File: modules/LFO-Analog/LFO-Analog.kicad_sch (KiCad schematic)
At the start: 56 parts, among them Q1 2N3904, Q2 2N3904, Q3 2N3904, Q4 2N3904, U1 TL074, U2 TL074

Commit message: LFO-Analog: BOM testing - it works!
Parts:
- RV1, RV2: Label (none) -> [label]
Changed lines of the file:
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@@
 			)
 		)
-		(property "Description" ""
+		(property "Description" "Resistor"
 			(at 207.01 38.1 0)
 			(effects
@@
 			)
 		)
-		(property "Description" ""
+		(property "Description" "Resistor"
 			(at 143.51 124.46 0)
 			(effects
@@
 			)
 		)
-		(property "Description" ""
+		(property "Description" "Resistor"
 			(at 143.51 40.64 0)
 			(effects
@@
 			)
 		)
-		(property "Description" ""
+		(property "Description" "Resistor"
 			(at 153.67 40.64 0)
 			(effects
@@
 			)
 		)
-		(property "Description" ""
+		(property "Description" "Small Signal NPN Transistor, 0.2A Ic, 40V Vce, TO-92"
 			(at 140.97 139.7 0)
 			(effects
@@
 			)
 		)
-		(property "Description" ""
+		(property "Description" "Small Signal NPN Transistor, 0.2A Ic, 40V Vce, TO-92"
 			(at 156.21 139.7 0)
 			(effects
@@
 			)
 		)
-		(property "Description" ""
+		(property "Description" "Trim-potentiometer"
 			(at 148.59 76.2 0)
 			(effects
@@
 			)
 		)
-		(property "Label" ""
+		(property "Label" "[label]"
 			(at 148.59 73.4639 90)
 			(effects
@@
 			)
 		)
-		(property "Description" ""
+		(property "Description" "Resistor"
 			(at 207.01 116.84 0)
 			(effects
@@
 			)
 		)
-		(property "Description" ""
+		(property "Description" "Resistor"
 			(at 207.01 33.02 0)
 			(effects
@@
 			)
 		)
-		(property "Description" ""
+		(property "Description" "Resistor"
 			(at 148.59 85.09 0)
 			(effects
@@
 			)
 		)
-		(property "Description" ""
+		(property "Description" "Resistor"
 			(at 161.29 146.05 0)
 			(effects
@@
 			)
 		)
-		(property "Description" ""
+		(property "Description" "Small Signal NPN Transistor, 0.2A Ic, 40V Vce, TO-92"
 			(at 156.21 55.88 0)
 			(effects
@@
 			)
 		)
-		(property "Description" ""
+		(property "Description" "Trim-potentiometer"
 			(at 148.59 160.02 0)
 			(effects
@@
 			)
 		)
-		(property "Label" ""
+		(property "Label" "[label]"
 			(at 148.59 157.2839 90)
 			(effects
@@
 			)
 		)
-		(property "Description" ""
+		(property "Description" "Resistor"
 			(at 161.29 62.23 0)
 			(effects
@@
 			)
 		)
-		(property "Description" ""
+		(property "Description" "Resistor"
 			(at 207.01 121.92 0)
 			(effects
@@
 			)
 		)
-		(property "Description" ""
+		(property "Description" "Resistor"
 			(at 153.67 124.46 0)
 			(effects
@@
 			)
 		)
-		(property "Description" ""
+		(property "Description" "Small Signal NPN Transistor, 0.2A Ic, 40V Vce, TO-92"
 			(at 140.97 55.88 0)
 			(effects
@@
 			)
 		)
-		(property "Description" ""
+		(property "Description" "Resistor"
 			(at 148.59 168.91 0)
 			(effects

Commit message: LFO-Analog: BOM testing - update some fields
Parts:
- RV1, RV2: Label [label] -> SINE-ADJ
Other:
- moved on the sheet: R11, R31, RV1, RV2

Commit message: LFO-Analog: BOM - done
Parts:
- C1, C5: Distributor (none) -> Mouser; DistributorPartLink (none) -> https://www.mouser.ca/ProductDetail/KEMET/R82EC1330JE50J?qs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; DistributorPartNum (none) -> 80-R82EC1330JE50J; Manufacturer (none) -> KEMET; ManufacturerPartNum (none) -> R82EC1330JE50J; Note PPS for best results -> (none)
- C2, C6: Distributor (none) -> Mouser; DistributorPartLink (none) -> https://www.mouser.ca/ProductDetail/KEMET/R82DC3680Z360K?qs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; DistributorPartNum (none) -> 80-R82DC3680Z360K; Manufacturer (none) -> KEMET; ManufacturerPartNum (none) -> R82DC3680Z360K; Note PPS for best results -> (none)
- C3, C7: Distributor (none) -> Mouser; DistributorPartLink (none) -> https://www.mouser.ca/ProductDetail/Vishay-BC-Components/K4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; DistributorPartNum (none) -> 594-K470J15C0GF53L2; Manufacturer (none) -> Vishay; ManufacturerPartNum (none) -> K470J15C0GF53L2
- C4, C8: Distributor (none) -> Mouser; DistributorPartLink (none) -> https://www.mouser.ca/ProductDetail/KEMET/R82EC1330JE50J?qs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; DistributorPartNum (none) -> 80-R82EC1330JE50J; Manufacturer (none) -> KEMET; ManufacturerPartNum (none) -> R82EC1330JE50J
- R1, R21: DistributorPartLink https://www.mouser.ca/c/?m=YAGEO&power+rating=166+mW+(1%2f6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 -> https://www.mouser.ca/ProductDetail/YAGEO/MFR-12FTF52-300K?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; DistributorPartNum 603-MFR-12* -> 603-MFR-12FTF52-300K; ManufacturerPartNum MFR-12* -> MFR-12FTF52-300K
- R10, R30: DistributorPartLink https://www.mouser.ca/c/?m=YAGEO&power+rating=166+mW+(1%2f6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 -> https://www.mouser.ca/ProductDetail/YAGEO/MFR-12FTF52-220R?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; DistributorPartNum 603-MFR-12* -> 603-MFR-12FTF52-220R; ManufacturerPartNum MFR-12* -> MFR-12FTF52-220R
- R11, R31: DistributorPartLink https://www.mouser.ca/c/?m=YAGEO&power+rating=166+mW+(1%2f6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 -> https://www.mouser.ca/ProductDetail/YAGEO/MFR-12FTF52-68K?q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; DistributorPartNum 603-MFR-12* -> 603-MFR-12FTF52-68K; ManufacturerPartNum MFR-12* -> MFR-12FTF52-68K
- R12, R26, R29, R32, R6, R9: DistributorPartLink https://www.mouser.ca/c/?m=YAGEO&power+rating=166+mW+(1%2f6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 -> https://www.mouser.ca/ProductDetail/YAGEO/MFR-12FTF52-10K?q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; DistributorPartNum 603-MFR-12* -> 603-MFR-12FTF52-10K; ManufacturerPartNum MFR-12* -> MFR-12FTF52-10K
- R13, R33: DistributorPartLink https://www.mouser.ca/c/?m=YAGEO&power+rating=166+mW+(1%2f6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 -> https://www.mouser.ca/ProductDetail/YAGEO/MFR-12FTF52-470R?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; DistributorPartNum 603-MFR-12* -> 603-MFR-12FTF52-470R; ManufacturerPartNum MFR-12* -> MFR-12FTF52-470R
- R14, R15, R19, R34, R35, R39: DistributorPartLink https://www.mouser.ca/c/?m=YAGEO&power+rating=166+mW+(1%2f6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 -> https://www.mouser.ca/ProductDetail/YAGEO/MFR-12FTF52-36K?q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; DistributorPartNum 603-MFR-12* -> 603-MFR-12FTF52-36K; ManufacturerPartNum MFR-12* -> MFR-12FTF52-36K
- R17, R18, R37, R38: DistributorPartLink https://www.mouser.ca/c/?m=YAGEO&power+rating=166+mW+(1%2f6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 -> https://www.mouser.ca/ProductDetail/YAGEO/MFR-12FTF52-220K?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; DistributorPartNum 603-MFR-12* -> 603-MFR-12FTF52-220K; ManufacturerPartNum MFR-12* -> MFR-12FTF52-220K
- R2, R20, R22, R27, R40, R7: DistributorPartLink https://www.mouser.ca/c/?m=YAGEO&power+rating=166+mW+(1%2f6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 -> https://www.mouser.ca/ProductDetail/YAGEO/MFR-12FTF52-100K?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; DistributorPartNum 603-MFR-12* -> 603-MFR-12FTF52-100K; ManufacturerPartNum MFR-12* -> MFR-12FTF52-100K
- R23, R3: DistributorPartLink https://www.mouser.ca/c/?m=YAGEO&power+rating=166+mW+(1%2f6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 -> https://www.mouser.ca/ProductDetail/YAGEO/MFR-12FTF52-4M7?q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; DistributorPartNum 603-MFR-12* -> 603-MFR-12FTF52-4M7; ManufacturerPartNum MFR-12* -> MFR-12FTF52-4M7
- R24, R4: DistributorPartLink https://www.mouser.ca/c/?m=YAGEO&power+rating=166+mW+(1%2f6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 -> https://www.mouser.ca/ProductDetail/YAGEO/MFR-12FTF52-200K?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; DistributorPartNum 603-MFR-12* -> 603-MFR-12FTF52-200K; ManufacturerPartNum MFR-12* -> MFR-12FTF52-200K
- R25, R5: DistributorPartLink https://www.mouser.ca/c/?m=YAGEO&power+rating=166+mW+(1%2f6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 -> https://www.mouser.ca/ProductDetail/YAGEO/MFR-12FTF52-11K?q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; DistributorPartNum 603-MFR-12* -> 603-MFR-12FTF52-11K; ManufacturerPartNum MFR-12* -> MFR-12FTF52-11K
- R28, R8: DistributorPartLink https://www.mouser.ca/c/?m=YAGEO&power+rating=166+mW+(1%2f6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 -> https://www.mouser.ca/ProductDetail/YAGEO/MFR-12FTF52-2K2?q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; DistributorPartNum 603-MFR-12* -> 603-MFR-12FTF52-2K2; ManufacturerPartNum MFR-12* -> MFR-12FTF52-2K2
- RV1, RV2: DistributorPartLink https://www.mouser.ca/c/passive-components/potentiometers-t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 -> https://www.mouser.ca/ProductDetail/Bourns/PV36W253C01B00?q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; DistributorPartNum 652-3296Z-* -> 81-PV36W253C01B00; ManufacturerPartNum 3296X-* -> PV36W253C01B00

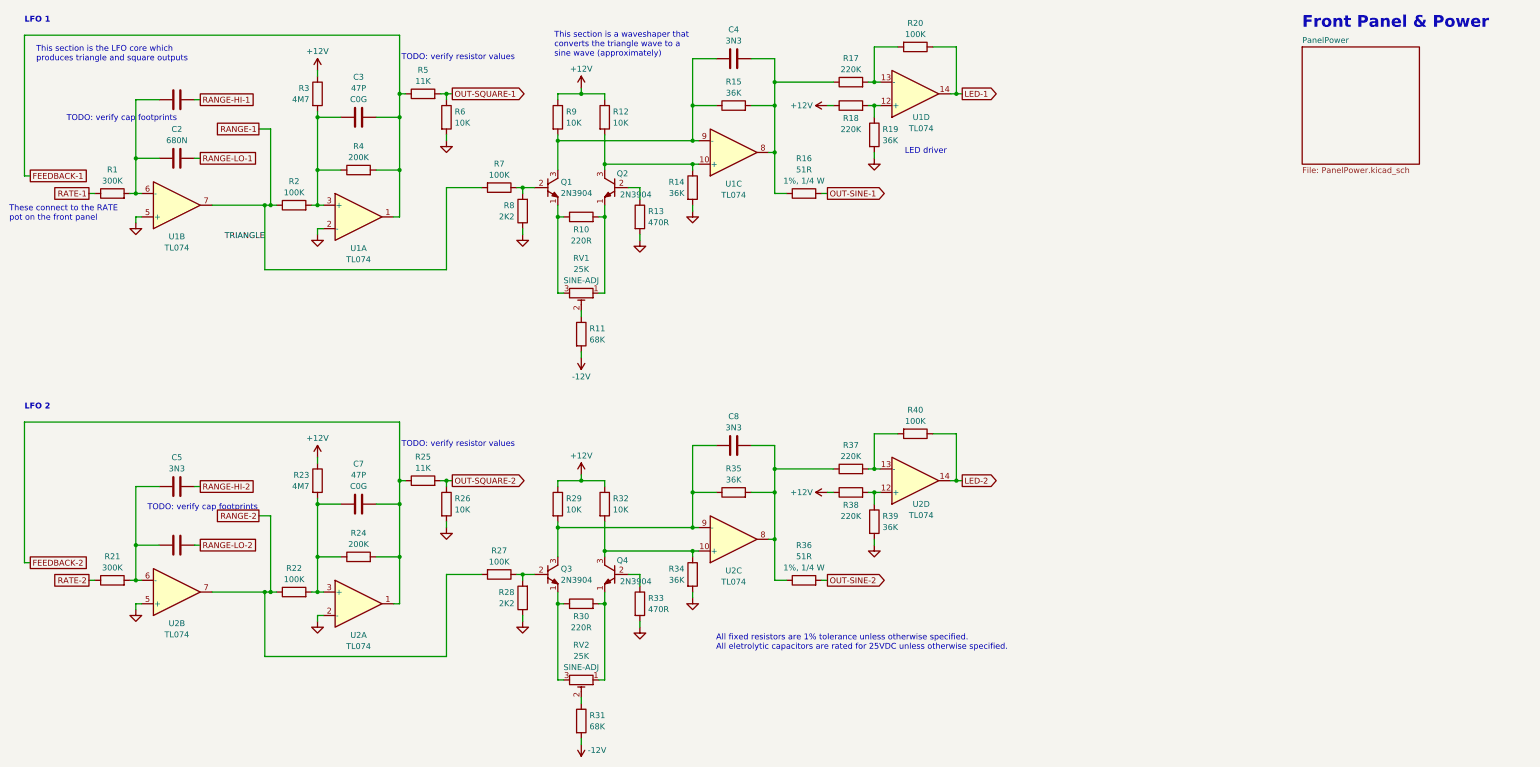
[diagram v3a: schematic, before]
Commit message: LFO-Analog: schematic tweaks
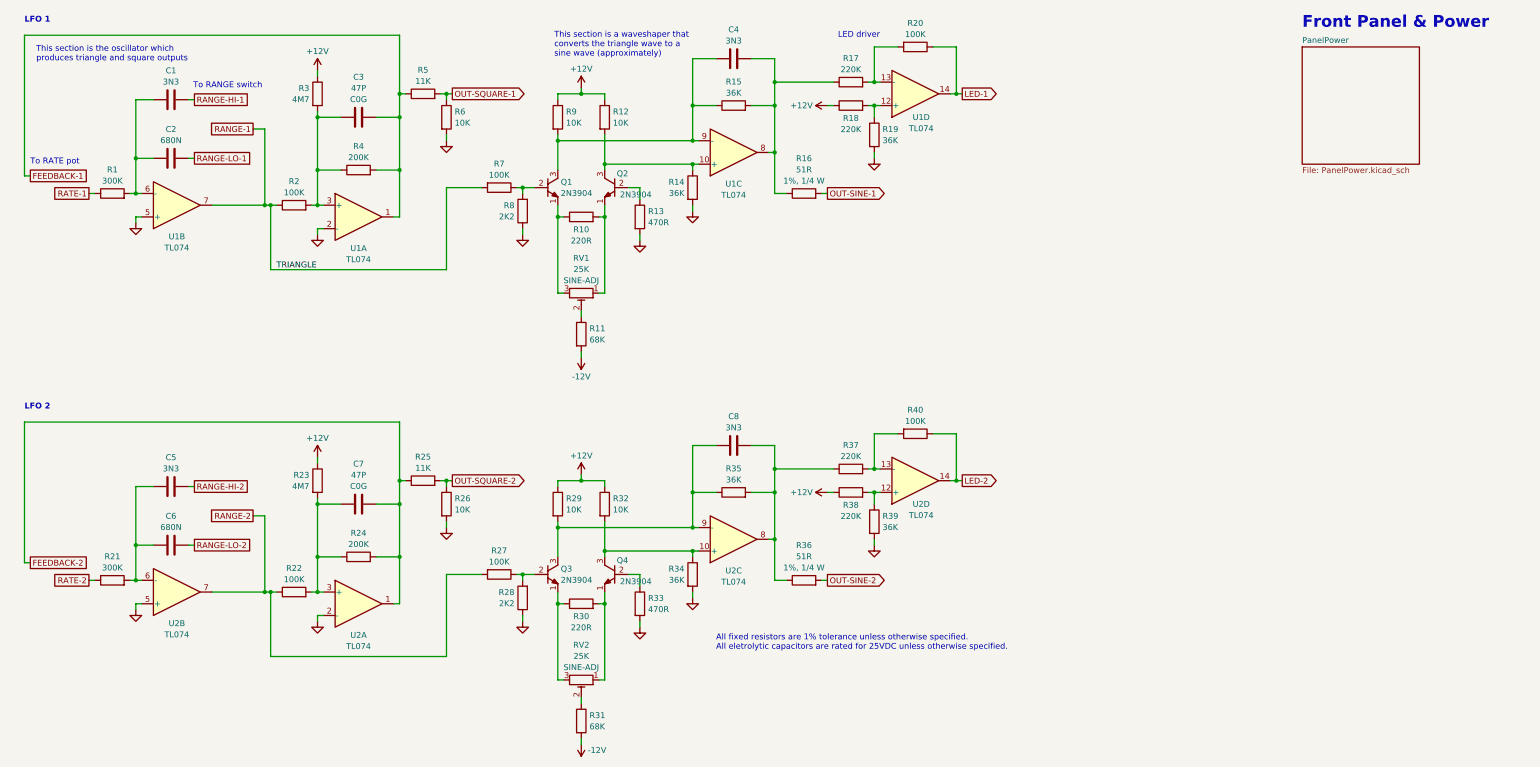
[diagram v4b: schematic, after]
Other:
- note added: "This section is the oscillator which produces triangle and square outputs"
- note added: "To RANGE switch"
- note added: "To RATE pot"
- note removed: "TODO: verify cap footprints"
- note removed: "TODO: verify resistor values"
- note removed: "These connect to the RATE pot on the front panel"
- note removed: "This section is the LFO core which produces triangle and square outputs"
- moved on the sheet: C2, C5
